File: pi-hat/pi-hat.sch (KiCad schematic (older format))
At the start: 79 parts, among them J1 Conn_01x04_Male, J2 Conn_01x04_Male, J3 Conn_01x05_Male, J4 Conn_01x05_Male, J5 Conn_01x05_Male, J7 Conn_01x07_Male, J8 Conn_01x07_Male, P1 Conn_02x20_Odd_Even, Q1 BSS138, Q10 AO 3415A, Q11 BC 818-25, Q12 BSS138, Q13 BSS138, Q14 BSS138, Q15 BSS138, Q16 BSS138, Q17 AO 3415A, Q2 BSS138, Q3 BSS138, Q4 BC 807-25, Q5 AO 3415A, Q6 BC 807-25, Q7 BC 818-25, Q8 BC 818-25, Q9 BC 818-25, U1 M24C02-WMN

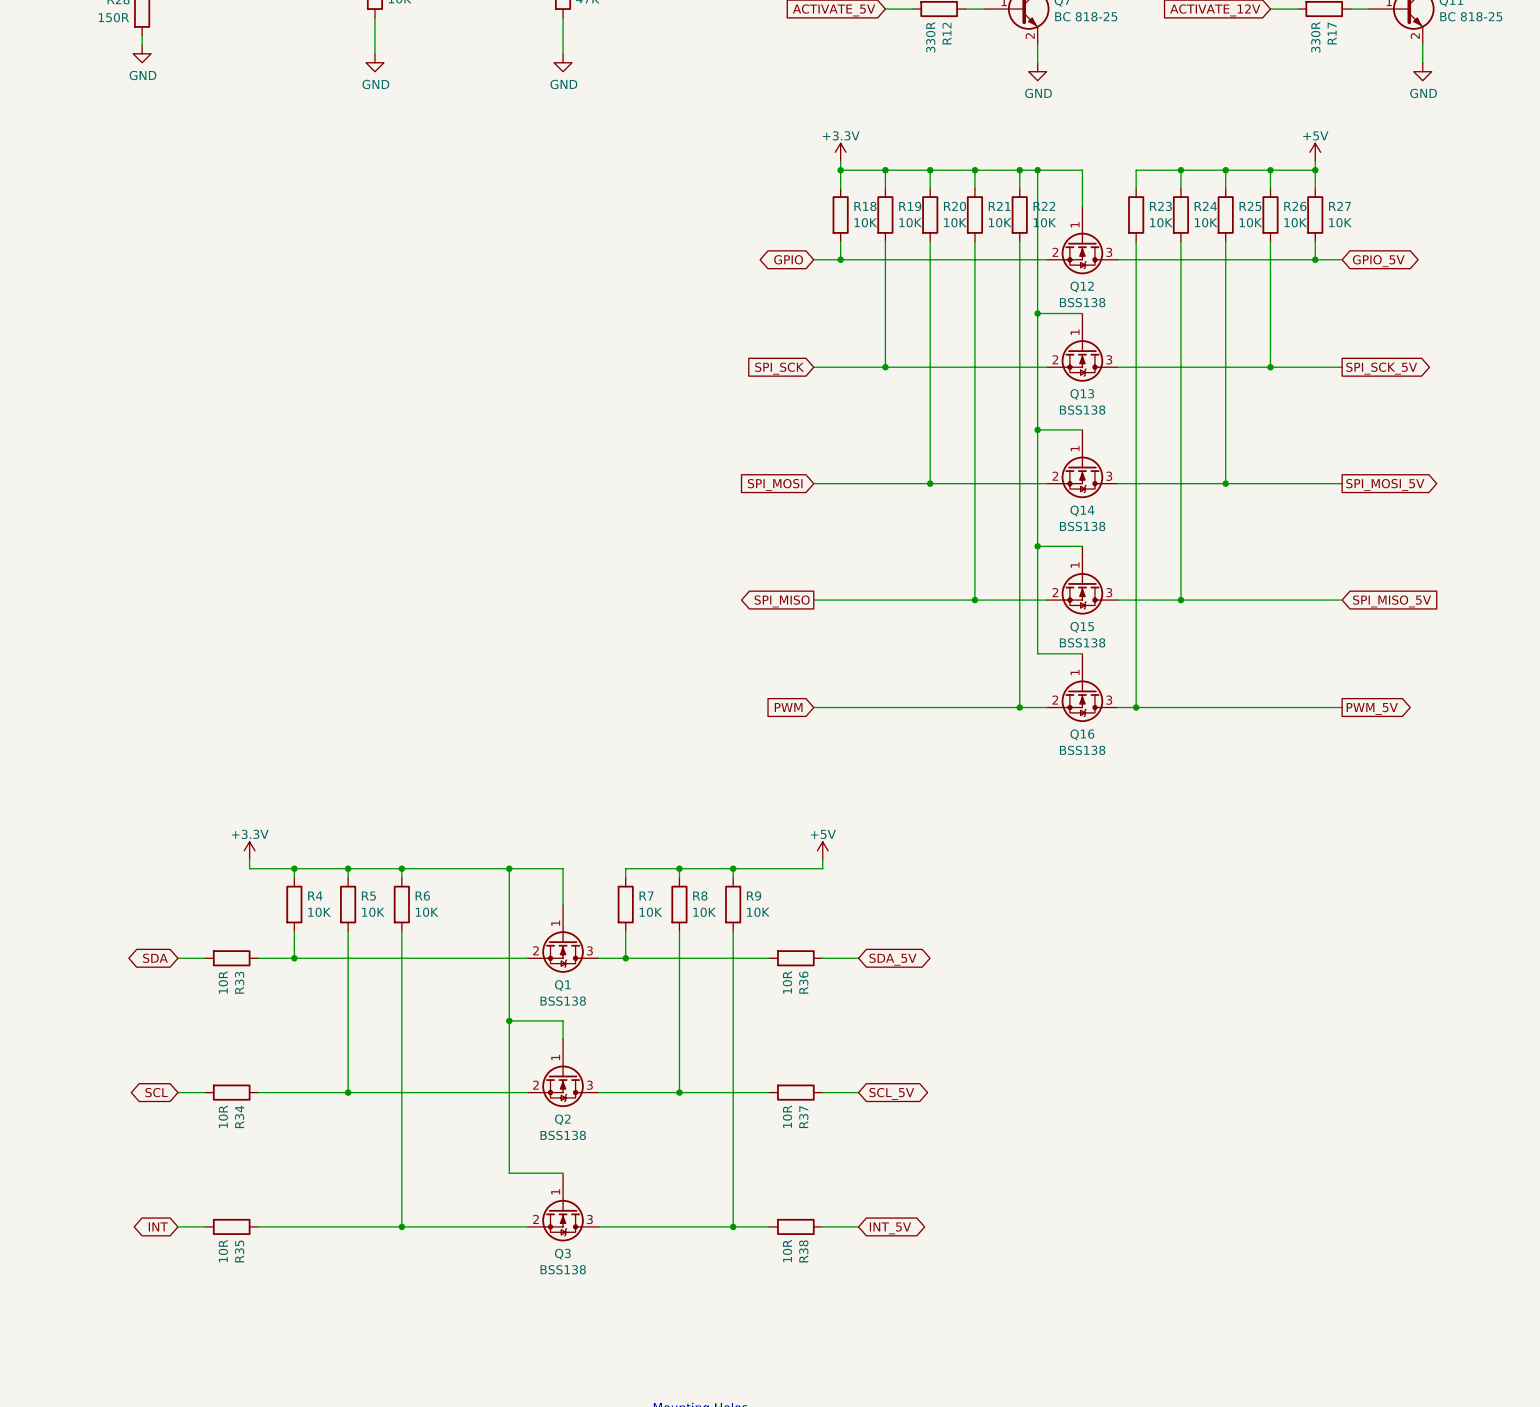
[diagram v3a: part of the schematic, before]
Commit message: Remove some level shifters
The level shifters made only sense for I3C - removed the rest.
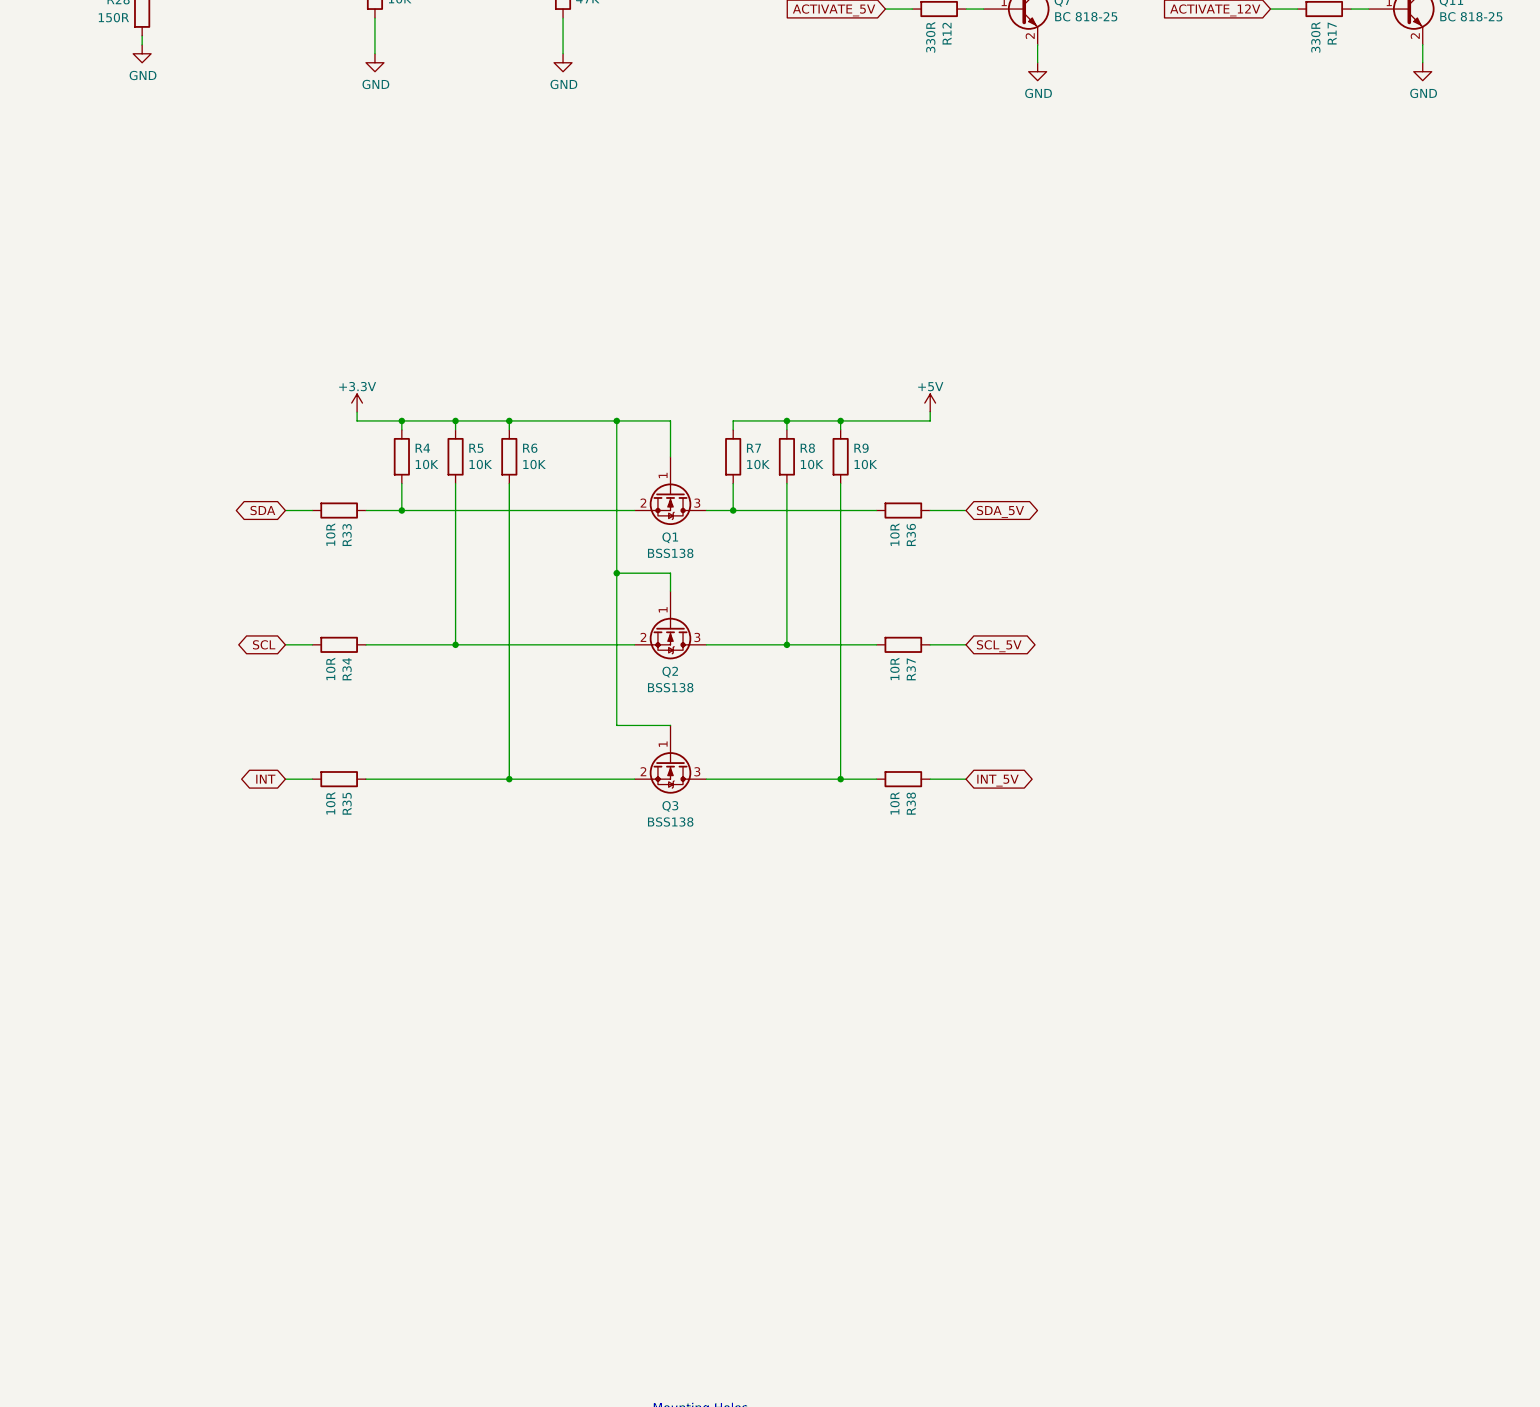
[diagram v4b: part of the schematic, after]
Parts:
- removed Q12, Q13, Q14, Q15, Q16: BSS138, Package_TO_SOT_SMD:SOT-23, symbol Transistor_FET:BSS138
- removed R18, R19, R20, R21, R22, R23, R24, R25, R26, R27: 10K, Capacitor_SMD:C_0603_1608Metric_Pad1.05x0.95mm_HandSolder, symbol Device:R
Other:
- moved on the sheet: Q1, Q2, Q3, R33, R34, R35, R36, R37, R38, R4, R5, R6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

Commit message: Run RenumKicadPCB to sort designators
https://github.com/penguineer/RenumKicadPCB
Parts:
- renumbered C3 to C1, C1 to C3, D2 to D1, D1 to D2, J8 to J1, J1 to J2, J7 to J3, J2 to J4, J3 to J5, J4 to J6, J5 to J7, MK5 to MK3, MK7 to MK4, MK6 to MK5, MK8 to MK6, MK3 to MK7, MK4 to MK8, Q5 to Q1, Q17 to Q10, Q7 to Q11, Q10 to Q12, Q1 to Q2, Q2 to Q3, Q3 to Q4, Q4 to Q5, Q8 to Q7, Q9 to Q8, Q11 to Q9, R11 to R10, R7 to R11, R8 to R12, R9 to R13, R10 to R14, R36 to R15, R37 to R16, R38 to R17, R15 to R18, R14 to R19, R31 to R20, R32 to R21, R17 to R22, R30 to R23, R29 to R24, R12 to R25, R16 to R26, R13 to R27, R33 to R4, R34 to R5, R35 to R6, R4 to R7, R5 to R8, R6 to R9
